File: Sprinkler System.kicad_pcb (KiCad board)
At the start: 2 copper layers, 154 x 85 mm, 63 parts, among them J1 Main Supply, J11 Station_0, J12 Station_1, J13 Station_2, J14 Station_3, J15 Station_4, J16 Station_5, J17 Conn_Button, J2 XFMR, J3 I2C, J4 UART0, K1 G3MB-202P, K11 G5LE-1, K12 G5LE-1, K13 G5LE-1, K14 G5LE-1, K15 G5LE-1, K16 G5LE-1, SW1 EN, SW2 BOOT, U1 HLK-PM01, U2 ULN2803A, U3 AMS1117-3.3, U4 ESP32-WROOM-32U

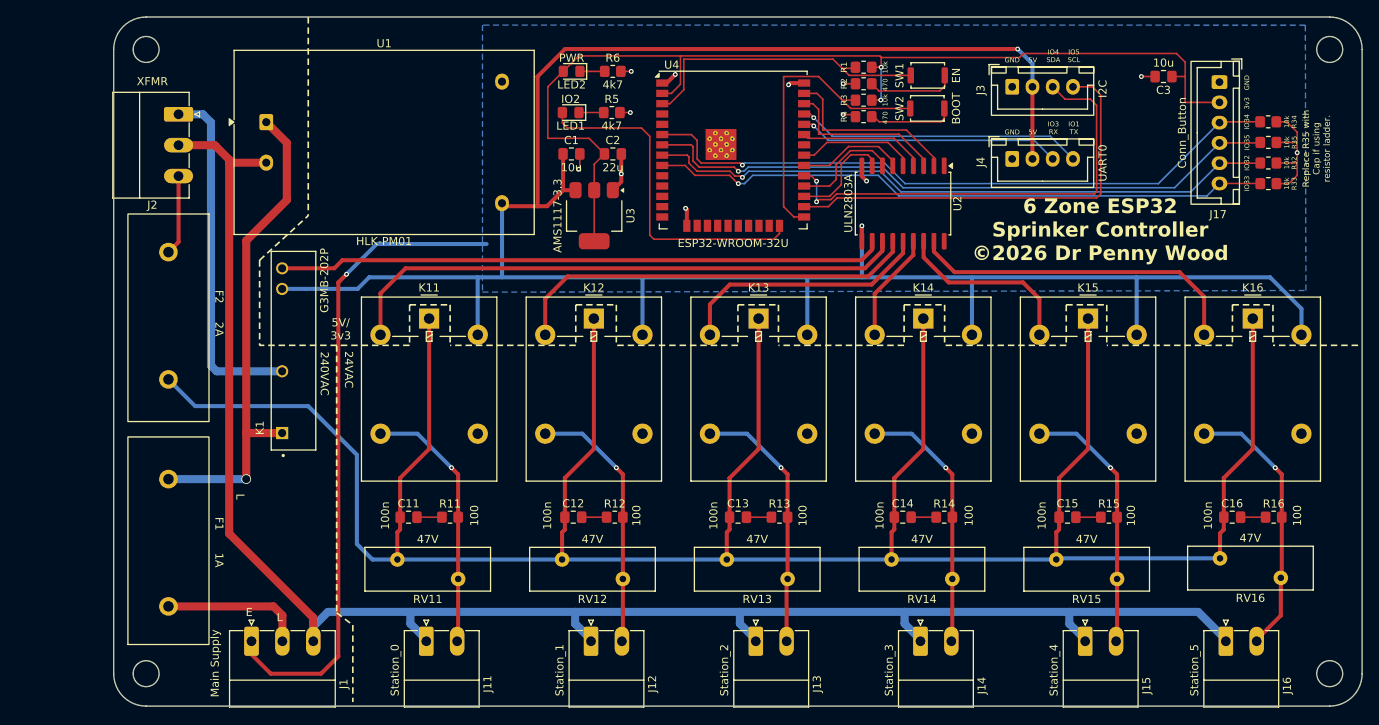
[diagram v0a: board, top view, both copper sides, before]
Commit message: feat: advance 6-zone sprinkler controller design and documentation
* replace template docs with full project README (safety notes, enclosure guidance, power/control paths, wiring, BOM, GPIO map)
* update schematic and PCB with major reannotation/layout changes, added test points, and 24 VAC net handling refinements
* add/update project rule settings (new 24VAC net class, net class priorities, DRC exclusion updates)
* adjust relay footprint 3D model orientation/offset
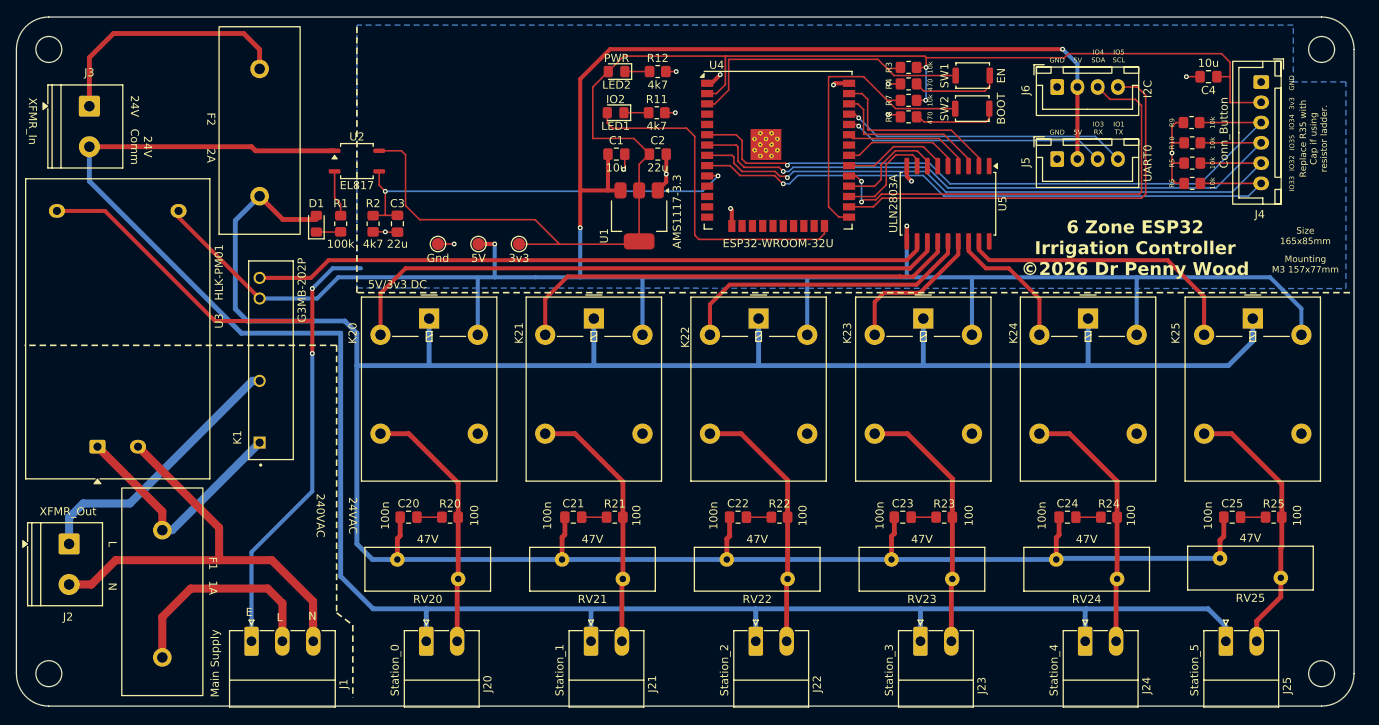
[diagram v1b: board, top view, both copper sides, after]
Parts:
- added C3: 22u, Capacitor_SMD:C_0805_2012Metric_Pad1.18x1.45mm_HandSolder, F.Cu at (100.0, 71.5)
- added D1: 1N4148, Diode_SMD:D_0805_2012Metric_Pad1.15x1.40mm_HandSolder, F.Cu at (90.0, 71.5)
- added J3: XFMR_In, TerminalBlock_Phoenix:TerminalBlock_Phoenix_PT-1,5-2-5.0-H_1x02_P5.00mm_Horizontal, F.Cu at (62.0, 57.0)
- added R1: 100k, Resistor_SMD:R_0805_2012Metric_Pad1.20x1.40mm_HandSolder, F.Cu at (93.0, 71.5)
- added R2: 4k7, Resistor_SMD:R_0805_2012Metric_Pad1.20x1.40mm_HandSolder, F.Cu at (97.0, 71.5)
- added TP1: Gnd, TestPoint:TestPoint_Pad_D1.5mm, F.Cu at (105.0, 74.0)
- added TP2: 5V, TestPoint:TestPoint_Pad_D1.5mm, F.Cu at (110.0, 74.0)
- added TP3: 3v3, TestPoint:TestPoint_Pad_D1.5mm, F.Cu at (115.0, 74.0)
- added U2: EL817, Package_SO:SOP-4_3.8x4.1mm_P2.54mm, F.Cu at (95.0, 63.8)
- J2: value XFMR -> XFMR_Out; footprint Connector_Phoenix_MC:PhoenixContact_MC_1,5_3-G-3.81_1x03_P3.81mm_Horizontal -> TerminalBlock_Phoenix:TerminalBlock_Phoenix_PT-1,5-2-5.0-H_1x02_P5.00mm_Horizontal
- moved J2 54.7 mm to (59.5, 111.0)
- moved U3 45.1 mm to (63.0, 99.0), turned to 90 degrees
- moved F2 13.2 mm to (83.0, 68.1), turned to 90 degrees
- moved REF** 12.0 mm to (57.0, 127.0)
- moved REF** 12.0 mm to (57.0, 50.0)
- moved R9 9.46 mm to (198.0, 59.0), turned to 180 degrees
- moved R10 9.38 mm to (198.0, 61.5), turned to 180 degrees
- moved R6 9.38 mm to (198.0, 66.5), turned to 180 degrees
- moved R5 9.38 mm to (198.0, 64.0), turned to 180 degrees
- moved F1 6.35 mm to (71.0, 125.0)
- moved C2 5.55 mm to (132.1, 62.9)
- moved SW1 5.55 mm to (171.0, 53.2)
- moved U1 5.55 mm to (129.8, 70.5)
- moved U5 5.55 mm to (167.9, 69.0)
- moved C1 5.55 mm to (127.0, 62.9)
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- renumbered C11 to C20, C12 to C21, C13 to C22, C14 to C23, C15 to C24, C16 to C25, C3 to C4, J11 to J20, J12 to J21, J13 to J22, J14 to J23, J15 to J24, J16 to J25, J17 to J4, J4 to J5, J3 to J6, K11 to K20, K12 to K21, K13 to K22, K14 to K23, K15 to K24, K16 to K25, R35 to R10, R5 to R11, R6 to R12, R11 to R20, R12 to R21, R13 to R22, R14 to R23, R15 to R24, R16 to R25, R1 to R3, R2 to R4, R32 to R5, R33 to R6, R3 to R7, R4 to R8, R34 to R9, RV11 to RV20, RV12 to RV21, RV13 to RV22, RV14 to RV23, RV15 to RV24, RV16 to RV25, U3 to U1, U1 to U3, U2 to U5
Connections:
- F2 pad 1: 24VAC_Supply -> 24VAC
- F2 pad 2: 24VAC -> 24V_Supply
- J20 pad 1: Neut -> 24V_Comm
- J21 pad 1: Neut -> 24V_Comm
- J22 pad 1: Neut -> 24V_Comm
- J23 pad 1: Neut -> 24V_Comm
- J24 pad 1: Neut -> 24V_Comm
- J25 pad 1: Neut -> 24V_Comm
- U4 pad 10: unconnected-(U4-IO25-Pad10) -> /Sens_24V
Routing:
- net 24V_Comm: track 0.00 -> 237.0 mm
- net Neut: track 212.5 -> 56.3 mm
- net /Sens_24V: track 0.00 -> 52.4 mm, vias 0 -> 2
- net +3V3: track 131.0 -> 176.6 mm
- net 24V_Supply: track 0.00 -> 31.4 mm
- net L: track 61.2 -> 30.1 mm, vias 1 -> 0
- net +5V: track 289.5 -> 308.3 mm, vias 2 -> 4
- net 24VAC: track 332.8 -> 348.6 mm
- net GND: track 119.9 -> 131.3 mm, vias 13 -> 16
- net 24VAC_Supply: track 9.90 -> 0.00 mm
- net L_SW: track 43.5 -> 33.7 mm
- net L_Supply: track 17.7 -> 26.7 mm
- net /SSR: track 74.8 -> 83.6 mm
- net /Coil4: track 22.8 -> 16.8 mm
- net Net-(R1-Pad1): track 0.00 -> 5.72 mm
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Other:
- board size 154 x 85 mm -> 165 x 85 mm
- board text added: "24V"
- board text added: "24V Comm"
- board text added: "5V/3v3 DC"
- board text added: "6 Zone ESP32 Irrigation Controller ©2026 Dr Penny Wood"
- board text added: "Mounting M3 157x77mm"
- board text added: "N"
- board text added: "Size 165x85mm"
- board text removed: "5V/ 3v3"
- board text removed: "6 Zone ESP32 Sprinker Controller ©2026 Dr Penny Wood"

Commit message: Update PCB layout, schematic, and project config
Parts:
- added R13: 4k7, Resistor_SMD:R_0805_2012Metric_Pad1.20x1.40mm_HandSolder, F.Cu at (198.0, 54.0)
- added R14: 4k7, Resistor_SMD:R_0805_2012Metric_Pad1.20x1.40mm_HandSolder, F.Cu at (198.0, 56.5)
- K20, K21, K22, K23, K24, K25: value G5LE-1 -> G5LE-1-DC5
- R1: value 100k -> 10k
- RV20, RV21, RV22, RV23, RV24, RV25: value 47V -> 68V
- moved C4 2.77 mm to (198.0, 51.5)
- renumbered REF** to H1, REF** to H2, REF** to H3, REF** to H4
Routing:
- net /SDA: track 56.4 -> 68.1 mm
- net /SCL: track 53.3 -> 58.0 mm
- net GND: track 131.3 -> 132.1 mm
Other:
- board text added: "Replace R10 with Cap if using resistor ladder."
- board text removed: "Replace R35 with Cap if using resistor ladder."
